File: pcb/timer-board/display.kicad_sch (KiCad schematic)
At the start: 1 part

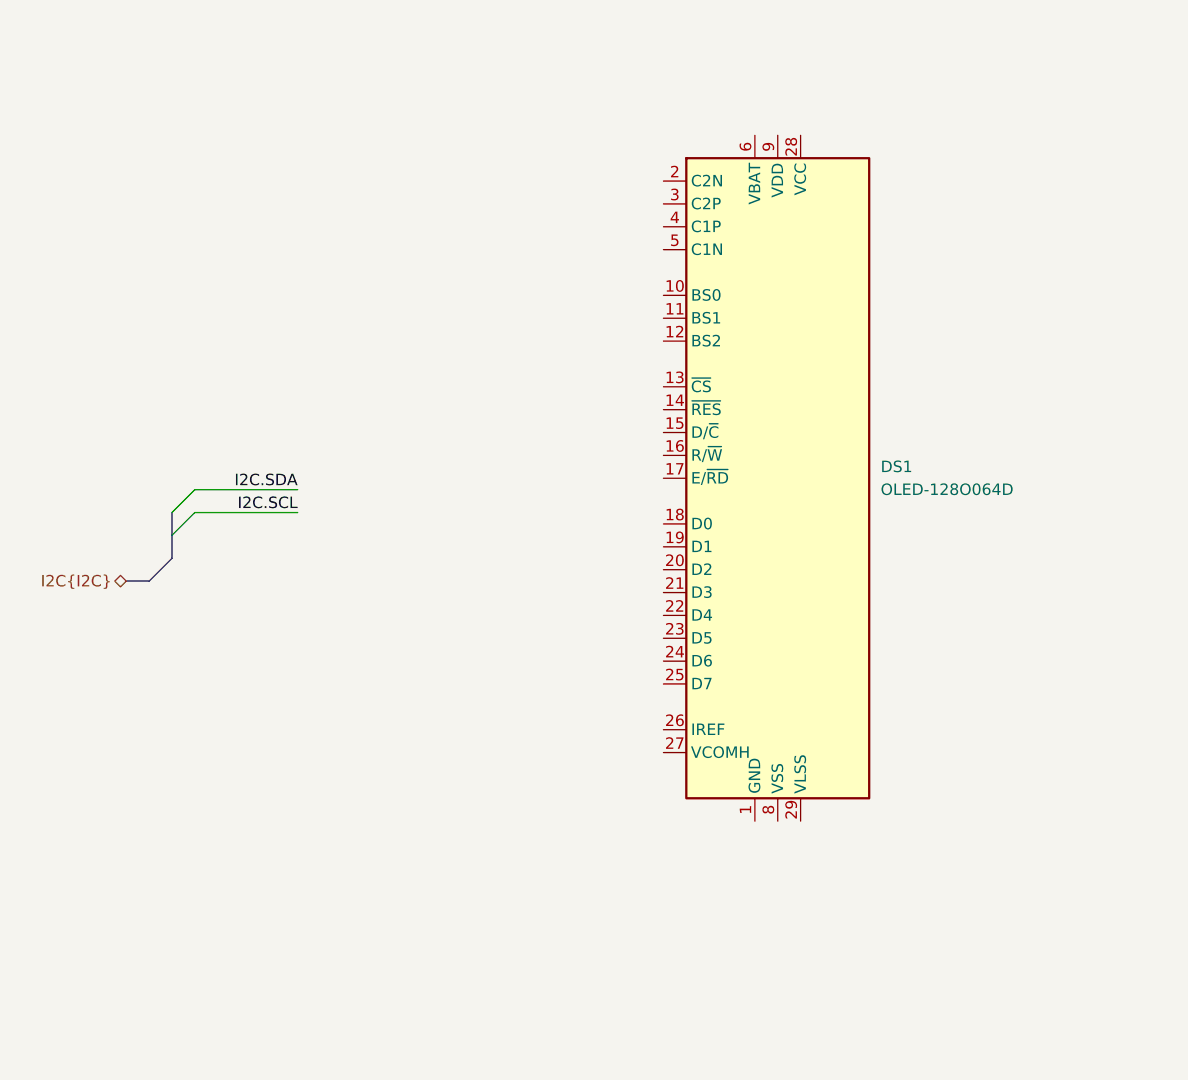
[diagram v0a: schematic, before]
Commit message: Connect OLED display, position main components
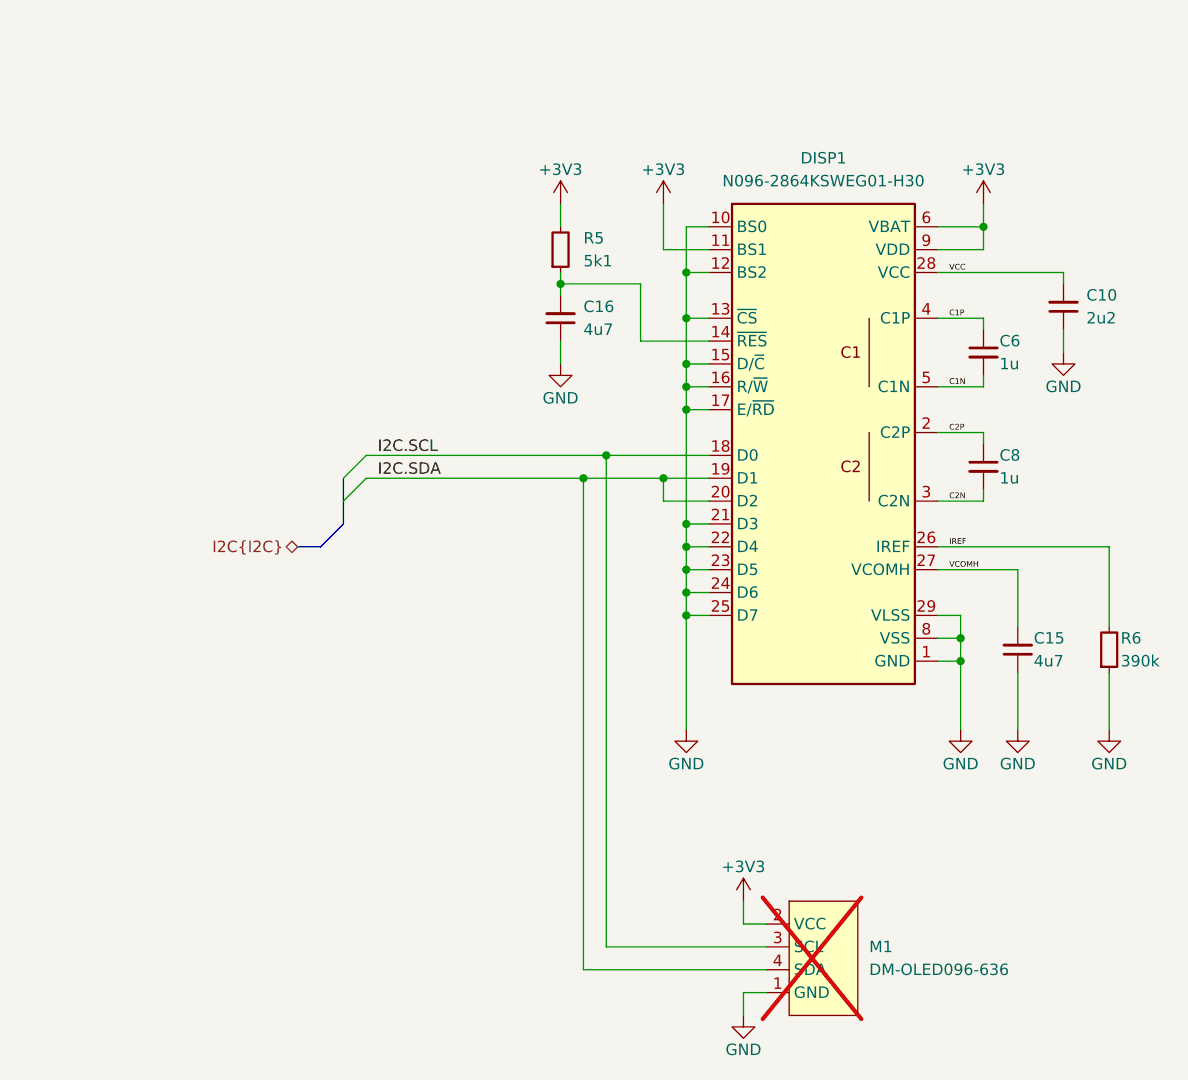
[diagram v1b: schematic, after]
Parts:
- removed DS1: OLED-128O064D, Display:OLED-128O064D, symbol Display_Graphic:OLED-128O064D
- added C10: C-2u2-0402, DW-footprints:C_0402_1005Metric, symbol DW-capacitors:C-2u2-0402
- added C15, C16: C-4u7-0402, DW-footprints:C_0402_1005Metric, symbol DW-capacitors:C-4u7-0402
- added C6, C8: C-1u-0402, DW-footprints:C_0402_1005Metric, symbol DW-capacitors:C-1u-0402
- added DISP1: N096-2864KSWEG01-H30, DW-footprints:N096-2864KSWEG01-H30, symbol DW-mechanical:N096-2864KSWEG01-H30
- added M1: DM-OLED096-636, DW-footprints:DM-OLED096-636, symbol DW-mechanical:DM-OLED096-636
- added R5: R-5k1-0402, DW-footprints:R_0402_1005Metric, symbol DW-resistors:R-5k1-0402
- added R6: R-390k-0402, DW-footprints:R_0402_1005Metric, symbol DW-resistors:R-390k-0402
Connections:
- net I2C.SCL: now also DISP1.18 (D0), M1.3 (SCL)
- net I2C.SDA: now also DISP1.19 (D1), DISP1.20 (D2), M1.4 (SDA)
- new net: C16.2, DISP1.14 (~{RES}), R5.1
- new net +3V3: DISP1.11 (BS1), DISP1.6 (VBAT), DISP1.9 (VDD), M1.2 (VCC), R5.2
- new net C1N: C6.2, DISP1.5 (C1N)
- new net C1P: C6.1, DISP1.4 (C1P)
- new net C2N: C8.2, DISP1.3 (C2N)
- new net C2P: C8.1, DISP1.2 (C2P)
- new net GND: C10.1, C15.1, C16.1, DISP1.1 (GND), DISP1.10 (BS0), DISP1.12 (BS2), DISP1.13 (~{CS}), DISP1.15 (D/~{C}), DISP1.16 (R/~{W}), DISP1.17 (E/~{RD}), DISP1.21 (D3), DISP1.22 (D4), DISP1.23 (D5), DISP1.24 (D6), DISP1.25 (D7), DISP1.29 (VLSS), DISP1.30 (GND), DISP1.8 (VSS), M1.1 (GND), R6.1
- new net IREF: DISP1.26 (IREF), R6.2
- new net VCC: C10.2, DISP1.28 (VCC)
- new net VCOMH: C15.2, DISP1.27 (VCOMH)

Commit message: Layout power planes and different signals
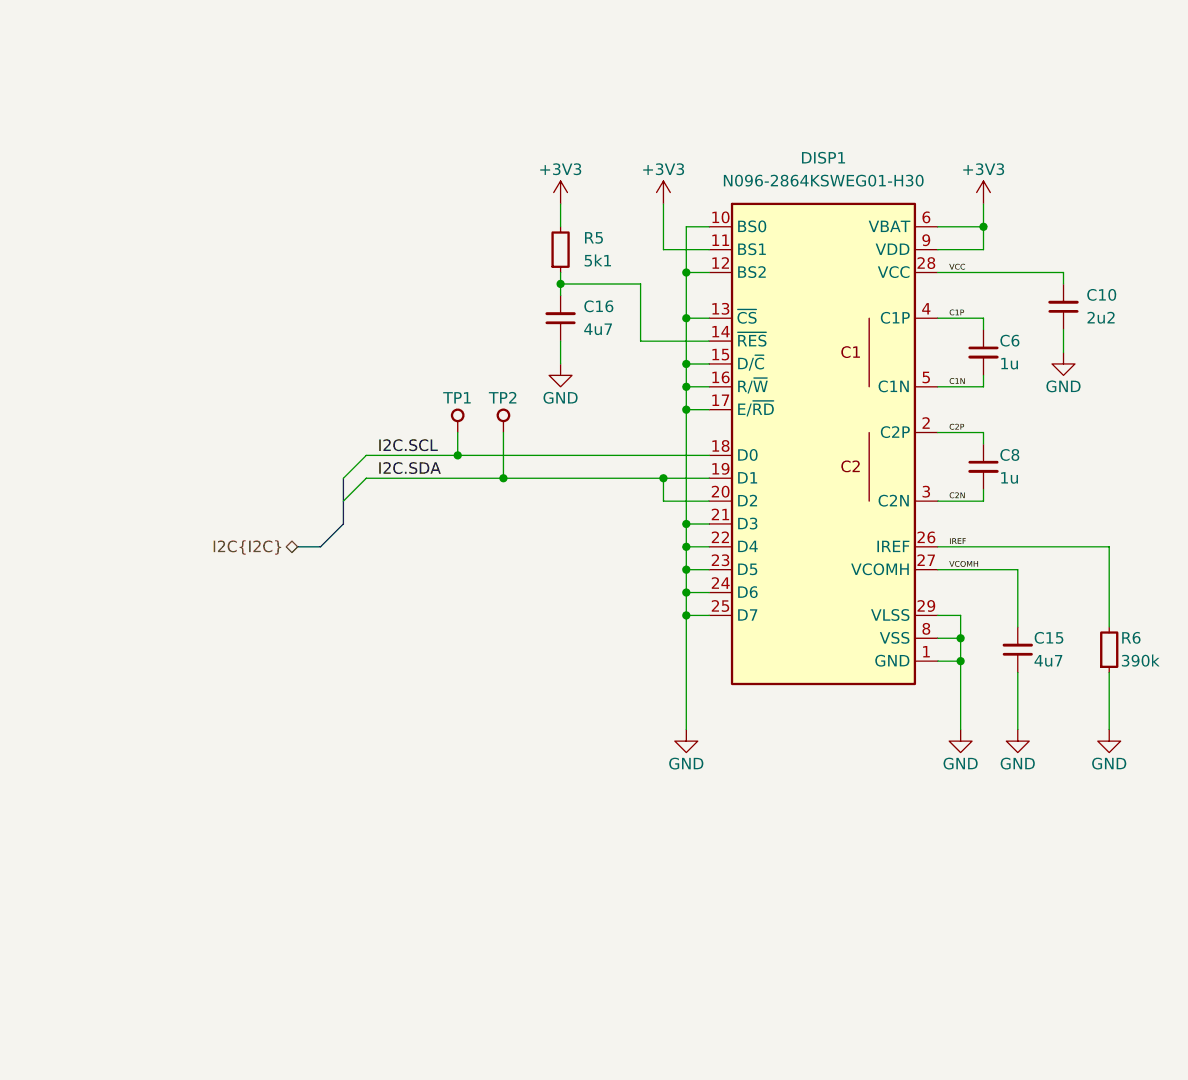
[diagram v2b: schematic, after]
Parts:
- removed M1: DM-OLED096-636, DW-footprints:DM-OLED096-636, symbol DW-mechanical:DM-OLED096-636
- added TP1, TP2: TP_SMD_1mm, DW-footprints:TP_SMD_1mm, symbol DW-test-points:TP_SMD_1mm
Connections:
- net I2C.SCL: now also TP1.1
- net I2C.SDA: now also TP2.1

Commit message: Finish uncompleted schematic sections, layout most of the PCB
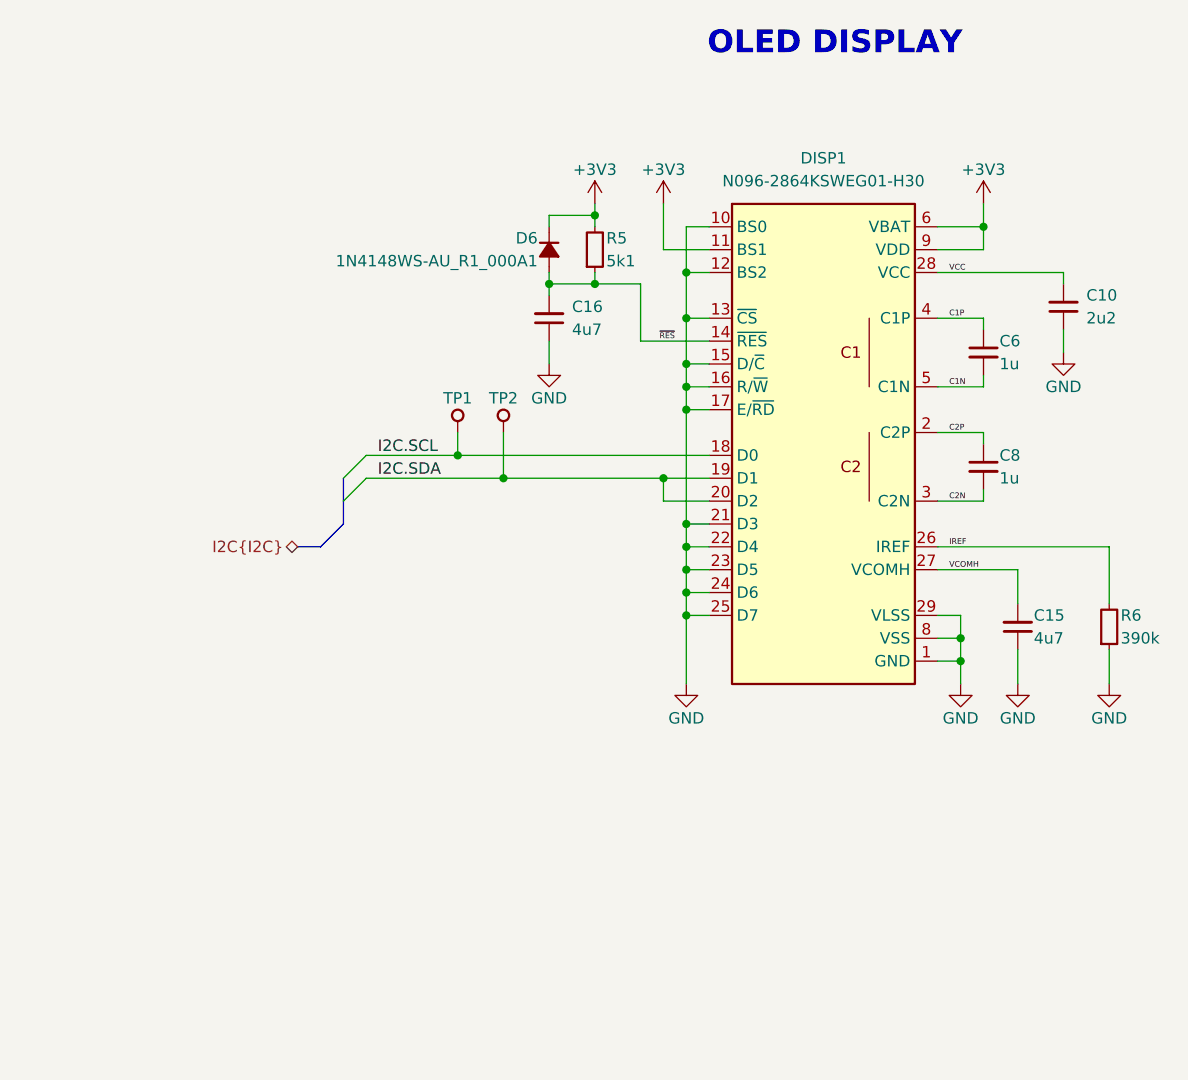
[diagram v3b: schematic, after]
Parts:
- added D6: 1N4148WS-AU, DW-footprints:D_SOD-323, symbol DW-diodes:1N4148WS-AU
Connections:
- net +3V3: now also D6.1 (C)
- net ~{RES}: now reaches C16.2, DISP1.14 (~{RES}), R5.1
- net ~{RES}: now also D6.2 (A)
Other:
- note added: "OLED DISPLAY"
- moved on the sheet: C15, C16, R5, R6

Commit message: Add I2C pull-up, IR receiver decoupling, LED labels, clear ERC and DRC
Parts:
- D6: footprint DW-footprints:D_SOD-323 -> DW-footprints:D_SOD-323F
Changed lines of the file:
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@@
+	)
+	(junction
+		(at 179.07 72.39)
+		(diameter 0)
+		(color 0 0 0 0)
 	)
 	(junction
@@
 		(pts
 			(xy 137.16 102.87) (xy 139.7 102.87)
+		)
+		(stroke
+			(width 0)
+			(type default)
+		)
+	)
+	(wire
+		(pts
+			(xy 179.07 71.12) (xy 179.07 72.39)
 		)
 		(stroke
@@
 			)
 		)
-		(property "Footprint" "DW-footprints:D_SOD-323"
+		(property "Footprint" "DW-footprints:D_SOD-323F"
 			(at 116.84 80.01 0)
 			(effects
@@
 					(unit 1)
 				)
+			)
+		)
+	)
+	(symbol
+		(lib_id "DW-power-symbols:PWR_FLAG")
+		(at 179.07 71.12 0)
+		(unit 1)
+		(exclude_from_sim no)
+		(in_bom yes)
+		(on_board yes)
+		(dnp no)
+		(property "Reference" "#FLG03"
+			(at 179.07 69.215 0)
+			(effects
+				(font
+					(size 1.27 1.27)
+				)
+				(hide yes)
+			)
+		)
+		(property "Value" "PWR_FLAG"
+			(at 179.07 67.31 0)
+			(effects
+				(font
+					(size 1.27 1.27)
+				)
+			)
+		)
+		(property "Footprint" ""
+			(at 179.07 71.12 0)
+			(effects
+				(font
+					(size 1.27 1.27)
+				)
+				(hide yes)
+			)
+		)
+		(property "Datasheet" "~"
+			(at 179.07 71.12 0)
+			(effects
+				(font
+					(size 1.27 1.27)
+				)
+				(hide yes)
+			)
+		)
+		(property "Description" "Special symbol for telling ERC where power comes from"
+			(at 179.07 71.12 0)
+			(effects
+				(font
+					(size 1.27 1.27)
+				)
+				(hide yes)
+			)
+		)
+		(pin "1"
+		)
+		(instances
+			(project "timer-board"
+				(path "/c6951331-127b-46f8-97b9-b4f2222f059c/778074c3-1cb0-4d0b-b940-338c86169e01"
+					(reference "#FLG03")
+					(unit 1)
+				)
